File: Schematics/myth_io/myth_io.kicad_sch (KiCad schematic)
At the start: 14 parts, among them J1 Conn_02x01, J1003 Conn_01x08_Pin, J1006 Conn_01x16_Pin, J1007 Conn_01x16_Pin, U1 74HC14, U1001 74AHC04, U2 74LS02, U3 74HC163, U4 74HC238, X1 CXO_DIP14

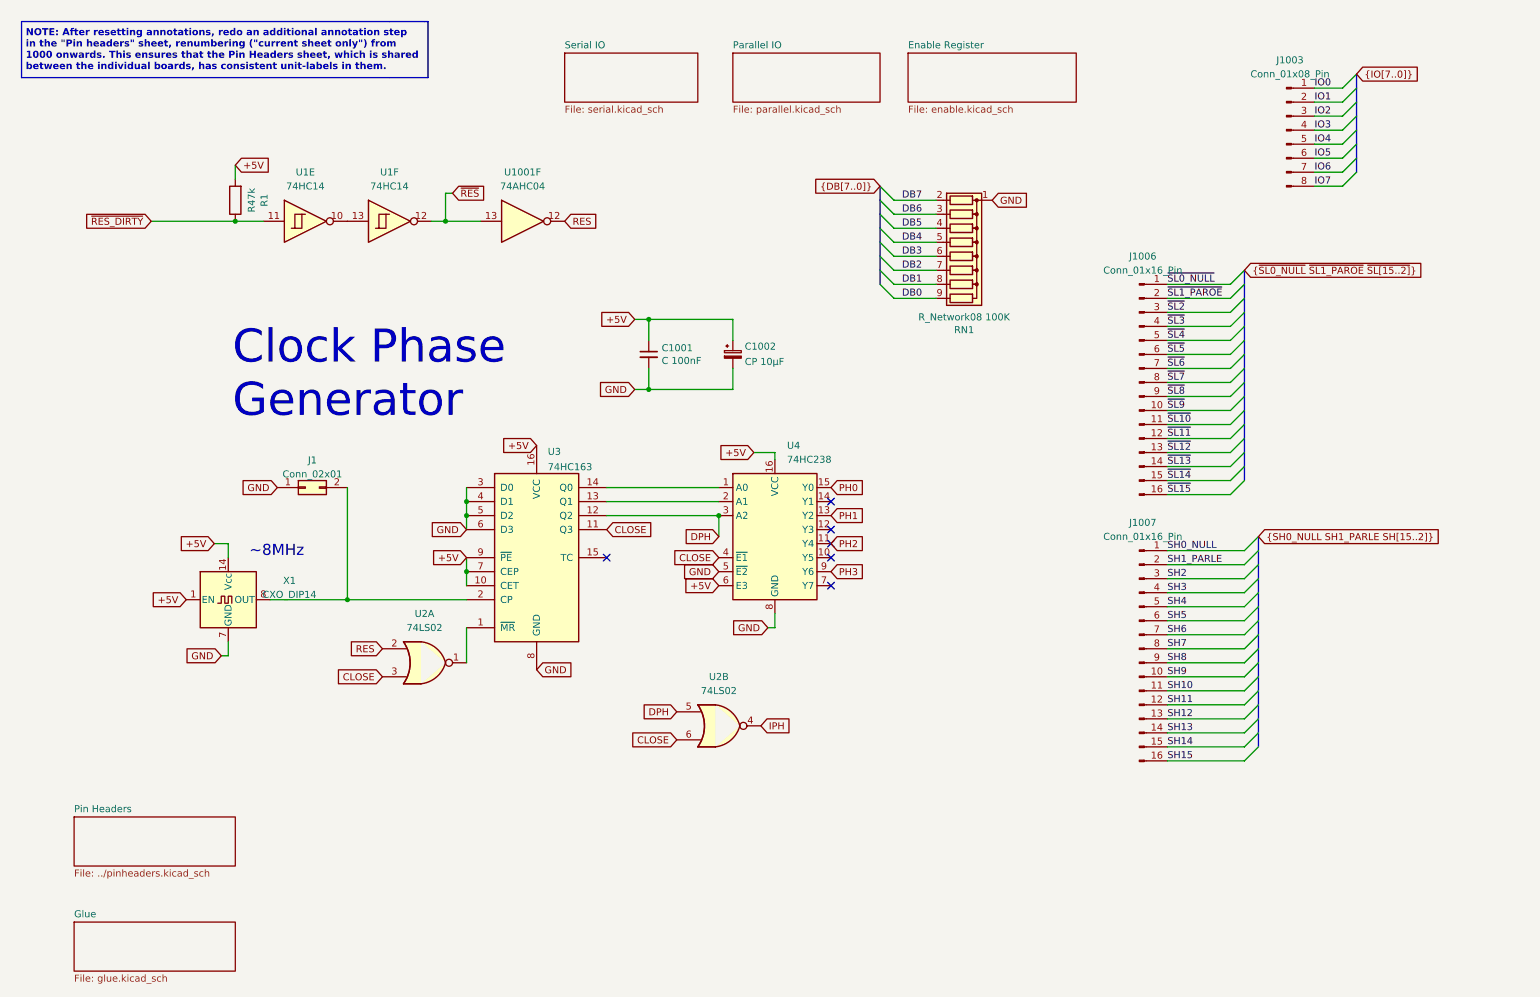
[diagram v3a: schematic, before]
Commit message: Change CO do D
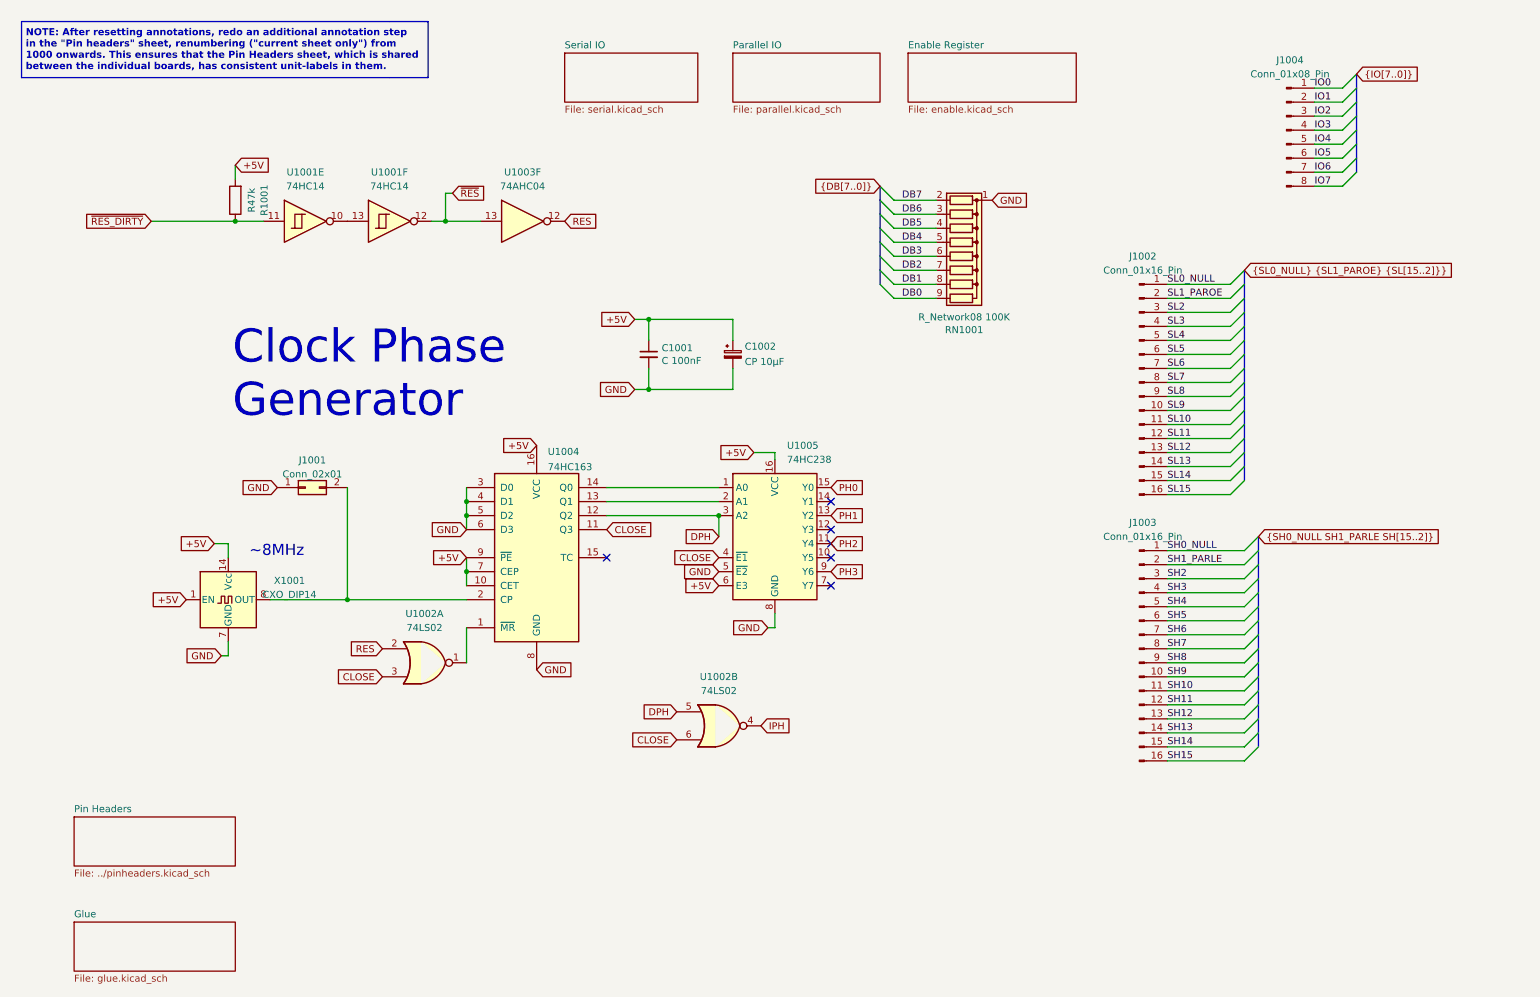
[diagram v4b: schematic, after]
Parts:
- renumbered J1 to J1001, J1006 to J1002, J1007 to J1003, J1003 to J1004, R1 to R1001, RN1 to RN1001, U1 to U1001, U2 to U1002, U1001 to U1003, U3 to U1004, U4 to U1005, X1 to X1001
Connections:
- net ~{SL0_NULL} renamed SL0_NULL
- net ~{SL10} renamed SL10
- net ~{SL11} renamed SL11
- net ~{SL12} renamed SL12
- net ~{SL13} renamed SL13
- net ~{SL14} renamed SL14
- net ~{SL15} renamed SL15
- net ~{SL1_PAROE} renamed SL1_PAROE
- net ~{SL2} renamed SL2
- net ~{SL3} renamed SL3
- net ~{SL4} renamed SL4
- net ~{SL5} renamed SL5
- net ~{SL6} renamed SL6
- net ~{SL7} renamed SL7
- net ~{SL8} renamed SL8
- net ~{SL9} renamed SL9
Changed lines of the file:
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@@
 		)
 	)
-	(label "~{SL2}"
+	(label "SL2"
 		(at 223.52 68.58 0)
 		(fields_autoplaced yes)
@@
 		)
 	)
-	(label "~{SL1_PAROE}"
+	(label "SL1_PAROE"
 		(at 223.52 66.04 0)
 		(fields_autoplaced yes)
@@
 		)
 	)
-	(label "~{SL10}"
+	(label "SL10"
 		(at 223.52 88.9 0)
 		(fields_autoplaced yes)
@@
 		)
 	)
-	(label "~{SL15}"
+	(label "SL15"
 		(at 223.52 101.6 0)
 		(fields_autoplaced yes)
@@
 		)
 	)
-	(label "~{SL9}"
+	(label "SL9"
 		(at 223.52 86.36 0)
 		(fields_autoplaced yes)
@@
 		)
 	)
-	(label "~{SL6}"
+	(label "SL6"
 		(at 223.52 78.74 0)
 		(fields_autoplaced yes)
@@
 		)
 	)
-	(label "~{SL11}"
+	(label "SL11"
 		(at 223.52 91.44 0)
 		(fields_autoplaced yes)
@@
 		)
 	)
-	(label "~{SL14}"
+	(label "SL14"
 		(at 223.52 99.06 0)
 		(fields_autoplaced yes)
@@
 		)
 	)
-	(label "~{SL12}"
+	(label "SL12"
 		(at 223.52 93.98 0)
 		(fields_autoplaced yes)
@@
 		)
 	)
-	(label "~{SL3}"
+	(label "SL3"
 		(at 223.52 71.12 0)
 		(fields_autoplaced yes)
@@
 		)
 	)
-	(label "~{SL8}"
+	(label "SL8"
 		(at 223.52 83.82 0)
 		(fields_autoplaced yes)
@@
 		)
 	)
-	(label "~{SL13}"
+	(label "SL13"
 		(at 223.52 96.52 0)
 		(fields_autoplaced yes)
@@
 		)
 	)
-	(label "~{SL0_NULL}"
+	(label "SL0_NULL"
 		(at 223.52 63.5 0)
 		(fields_autoplaced yes)
@@
 		)
 	)
-	(label "~{SL5}"
+	(label "SL5"
 		(at 223.52 76.2 0)
 		(fields_autoplaced yes)
@@
 		)
 	)
-	(label "~{SL7}"
+	(label "SL7"
 		(at 223.52 81.28 0)
 		(fields_autoplaced yes)
@@
 		)
 	)
-	(label "~{SL4}"
+	(label "SL4"
 		(at 223.52 73.66 0)
 		(fields_autoplaced yes)
@@
 		)
 	)
-	(global_label "{~{SL0_NULL} ~{SL1_PAROE} ~{SL[15..2]}}"
+	(global_label "{SL0_NULL} {SL1_PAROE} {SL[15..2]}}"
 		(shape input)
 		(at 237.49 60.96 0)
@@
 		)
 		(property "Intersheetrefs" "${INTERSHEET_REFS}"
-			(at 272.5276 60.96 0)
+			(at 276.7611 60.96 0)
 			(effects
 				(font
@@
 		(dnp no)
 		(fields_autoplaced yes)
-		(property "Reference" "U3"
+		(property "Reference" "U1004"
 			(at 111.2394 93.8235 0)
 			(effects
@@
 			(project "myth_io"
 				(path "/a907dd88-e0e4-4e6e-a291-053f6213a316"
-					(reference "U3")
+					(reference "U1004")
 					(unit 1)
 				)
@@
 		(dnp no)
 		(fields_autoplaced yes)
-		(property "Reference" "U1"
+		(property "Reference" "U1001"
 			(at 67.31 43.18 0)
 			(effects
@@
 			(project ""
 				(path "/a907dd88-e0e4-4e6e-a291-053f6213a316"
-					(reference "U1")
+					(reference "U1001")
 					(unit 5)
 				)
@@
 		(dnp no)
 		(fields_autoplaced yes)
-		(property "Reference" "J1003"
+		(property "Reference" "J1004"
 			(at 245.745 22.86 0)
 			(effects
@@
 			(project "myth_io"
 				(path "/a907dd88-e0e4-4e6e-a291-053f6213a316"
-					(reference "J1003")
+					(reference "J1004")
 					(unit 1)
 				)
@@
 		(dnp no)
 		(fields_autoplaced yes)
-		(property "Reference" "U4"
+		(property "Reference" "U1005"
 			(at 154.5941 92.71 0)
 			(effects
@@
 			(project ""
 				(path "/a907dd88-e0e4-4e6e-a291-053f6213a316"
-					(reference "U4")
+					(reference "U1005")
 					(unit 1)
 				)
@@
 		(dnp no)
 		(fields_autoplaced yes)
-		(property "Reference" "X1"
+		(property "Reference" "X1001"
 			(at 64.4321 117.1916 0)
 			(effects
@@
 			(project "myth_io"
 				(path "/a907dd88-e0e4-4e6e-a291-053f6213a316"
-					(reference "X1")
+					(reference "X1001")
 					(unit 1)
 				)
@@
 		(on_board yes)
 		(dnp no)
-		(property "Reference" "J1"
+		(property "Reference" "J1001"
 			(at 68.58 95.3602 0)
 			(effects
@@
 			(project "myth_io"
 				(path "/a907dd88-e0e4-4e6e-a291-053f6213a316"
-					(reference "J1")
+					(reference "J1001")
 					(unit 1)
 				)
@@
 		(dnp no)
 		(fields_autoplaced yes)
-		(property "Reference" "U1"
+		(property "Reference" "U1001"
 			(at 82.55 43.18 0)
 			(effects
@@
 			(project ""
 				(path "/a907dd88-e0e4-4e6e-a291-053f6213a316"
-					(reference "U1")
+					(reference "U1001")
 					(unit 6)
 				)
@@
 		(on_board yes)
 		(dnp no)
-		(property "Reference" "R1"
+		(property "Reference" "R1001"
 			(at 59.8678 48.26 90)
 			(effects
@@
 			(project "myth_io"
 				(path "/a907dd88-e0e4-4e6e-a291-053f6213a316"
-					(reference "R1")
+					(reference "R1001")
 					(unit 1)
 				)
@@
 		(dnp no)
 		(fields_autoplaced yes)
-		(property "Reference" "U2"
+		(property "Reference" "U1002"
 			(at 142.24 134.62 0)
 			(effects
@@
 			(project ""
 				(path "/a907dd88-e0e4-4e6e-a291-053f6213a316"
-					(reference "U2")
+					(reference "U1002")
 					(unit 2)
 				)
@@
 		(dnp no)
 		(fields_autoplaced yes)
-		(property "Reference" "J1007"
+		(property "Reference" "J1003"
 			(at 219.075 106.68 0)
 			(effects
@@
 			(project "myth_io"
 				(path "/a907dd88-e0e4-4e6e-a291-053f6213a316"
-					(reference "J1007")
+					(reference "J1003")
 					(unit 1)
 				)
@@
 		(dnp no)
 		(fields_autoplaced yes)
-		(property "Reference" "J1006"
+		(property "Reference" "J1002"
 			(at 219.075 58.42 0)
 			(effects
@@
 			(project "myth_io"
 				(path "/a907dd88-e0e4-4e6e-a291-053f6213a316"
-					(reference "J1006")
+					(reference "J1002")
 					(unit 1)
 				)
@@
 		(dnp no)
 		(fields_autoplaced yes)
-		(property "Reference" "U2"
+		(property "Reference" "U1002"
 			(at 88.9 123.19 0)
 			(effects
@@
 			(project ""
 				(path "/a907dd88-e0e4-4e6e-a291-053f6213a316"
-					(reference "U2")
+					(reference "U1002")
 					(unit 1)
 				)
@@
 		(on_board yes)
 		(dnp no)
-		(property "Reference" "RN1"
+		(property "Reference" "RN1001"
 			(at 186.69 71.755 90)
 			(effects
@@
 			(project "myth_io"
 				(path "/a907dd88-e0e4-4e6e-a291-053f6213a316"
-					(reference "RN1")
+					(reference "RN1001")
 					(unit 1)
 				)
@@
 		(dnp no)
 		(fields_autoplaced yes)
-		(property "Reference" "U1001"
+		(property "Reference" "U1003"
 			(at 106.68 43.18 0)
 			(effects
@@
 			(project "myth_io"
 				(path "/a907dd88-e0e4-4e6e-a291-053f6213a316"
-					(reference "U1001")
+					(reference "U1003")
 					(unit 6)
 				)

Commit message: Fix documentation re: change d->g
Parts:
- added C1001: C 100nF, Capacitor_THT:C_Disc_D5.0mm_W2.5mm_P2.50mm, symbol Device:C_Small
- renumbered C1001 to C1002, C1002 to C1003
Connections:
- net GND: now also C1001.2
- net ~{RES_DIRTY}: now also C1001.1
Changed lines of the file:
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@@
 	(wire
 		(pts
+			(xy 54.61 63.5) (xy 54.61 67.31)
+		)
+		(stroke
+			(width 0)
+			(type default)
+		)
+	)
+	(wire
+		(pts
 			(xy 127 69.85) (xy 129.54 69.85)
 		)
@@
 		)
 	)
+	(wire
+		(pts
+			(xy 54.61 52.07) (xy 54.61 58.42)
+		)
+		(stroke
+			(width 0)
+			(type default)
+		)
+	)
 	(bus
 		(pts
@@
 	(text "Clock Phase\nGenerator"
 		(exclude_from_sim no)
-		(at 54.102 88.138 0)
+		(at 66.802 85.852 0)
 		(effects
 			(font
-				(size 6 6)
+				(size 5.08 5.08)
 			)
 			(justify left bottom)
@@
 		)
 	)
+	(global_label "GND"
+		(shape input)
+		(at 54.61 67.31 0)
+		(fields_autoplaced yes)
+		(effects
+			(font
+				(size 1.27 1.27)
+			)
+			(justify left)
+		)
+		(property "Intersheetrefs" "${INTERSHEET_REFS}"
+			(at 61.4657 67.31 0)
+			(effects
+				(font
+					(size 1.27 1.27)
+				)
+				(justify left)
+				(hide yes)
+			)
+		)
+	)
 	(symbol
 		(lib_id "74xx:74LS163")
@@
 		(on_board yes)
 		(dnp no)
-		(property "Reference" "C1001"
+		(property "Reference" "C1002"
 			(at 131.8768 75.0316 0)
 			(effects
@@
 			(project "myth_io"
 				(path "/a907dd88-e0e4-4e6e-a291-053f6213a316"
-					(reference "C1001")
+					(reference "C1002")
 					(unit 1)
 				)
@@
 	)
 	(symbol
+		(lib_id "Device:C_Small")
+		(at 54.61 60.96 0)
+		(unit 1)
+		(exclude_from_sim no)
+		(in_bom yes)
+		(on_board yes)
+		(dnp no)
+		(property "Reference" "C1001"
+			(at 56.9468 59.7916 0)
+			(effects
+				(font
+					(size 1.27 1.27)
+				)
+				(justify left)
+			)
+		)
+		(property "Value" "C 100nF"
+			(at 56.9468 62.103 0)
+			(effects
+				(font
+					(size 1.27 1.27)
+				)
+				(justify left)
+			)
+		)
+		(property "Footprint" "Capacitor_THT:C_Disc_D5.0mm_W2.5mm_P2.50mm"
+			(at 54.61 60.96 0)
+			(effects
+				(font
+					(size 1.27 1.27)
+				)
+				(hide yes)
+			)
+		)
+		(property "Datasheet" "~"
+			(at 54.61 60.96 0)
+			(effects
+				(font
+					(size 1.27 1.27)
+				)
+				(hide yes)
+			)
+		)
+		(property "Description" ""
+			(at 54.61 60.96 0)
+			(effects
+				(font
+					(size 1.27 1.27)
+				)
+				(hide yes)
+			)
+		)
+		(pin "1"
+		)
+		(pin "2"
+		)
+		(instances
+			(project "myth_io"
+				(path "/a907dd88-e0e4-4e6e-a291-053f6213a316"
+					(reference "C1001")
+					(unit 1)
+				)
+			)
+		)
+	)
+	(symbol
 		(lib_id "Device:R")
 		(at 54.61 48.26 180)
@@
 		(dnp no)
 		(fields_autoplaced yes)
-		(property "Reference" "C1002"
+		(property "Reference" "C1003"
 			(at 146.939 74.7454 0)
 			(effects
@@
 			(project "myth_io"
 				(path "/a907dd88-e0e4-4e6e-a291-053f6213a316"
-					(reference "C1002")
+					(reference "C1003")
 					(unit 1)
 				)
